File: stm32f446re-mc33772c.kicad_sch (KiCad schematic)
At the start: 43 parts, among them J1 Conn_01x02, J2 USB_B_Micro, J3 Conn_01x03, J4 Conn_01x03, J6 SM06B-GHS-TB, U1 STM32F446RETx, U3 LD1086D2M33TR, U4 AMS1117-3.3, U6 LMR51450SDRRR, U7 SN65HVD232, Y1 16MHz

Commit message: no error in DRC
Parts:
- J1: footprint Connector_PinHeader_1.00mm:PinHeader_1x02_P1.00mm_Vertical -> Connector_PinHeader_2.54mm:PinHeader_1x02_P2.54mm_Vertical
- J3, J4: footprint Connector_PinHeader_1.00mm:PinHeader_1x03_P1.00mm_Vertical -> Connector_PinHeader_2.54mm:PinHeader_1x03_P2.54mm_Vertical
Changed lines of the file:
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@@
 			)
 		)
-		(property "Footprint" "Connector_PinHeader_1.00mm:PinHeader_1x03_P1.00mm_Vertical"
+		(property "Footprint" "Connector_PinHeader_2.54mm:PinHeader_1x03_P2.54mm_Vertical"
 			(at 148.59 176.53 0)
 			(hide yes)
@@
 			)
 		)
-		(property "Footprint" "Connector_PinHeader_1.00mm:PinHeader_1x02_P1.00mm_Vertical"
+		(property "Footprint" "Connector_PinHeader_2.54mm:PinHeader_1x02_P2.54mm_Vertical"
 			(at 41.91 97.79 0)
 			(hide yes)
@@
 			)
 		)
-		(property "Footprint" "Connector_PinHeader_1.00mm:PinHeader_1x03_P1.00mm_Vertical"
+		(property "Footprint" "Connector_PinHeader_2.54mm:PinHeader_1x03_P2.54mm_Vertical"
 			(at 127 27.94 0)
 			(hide yes)

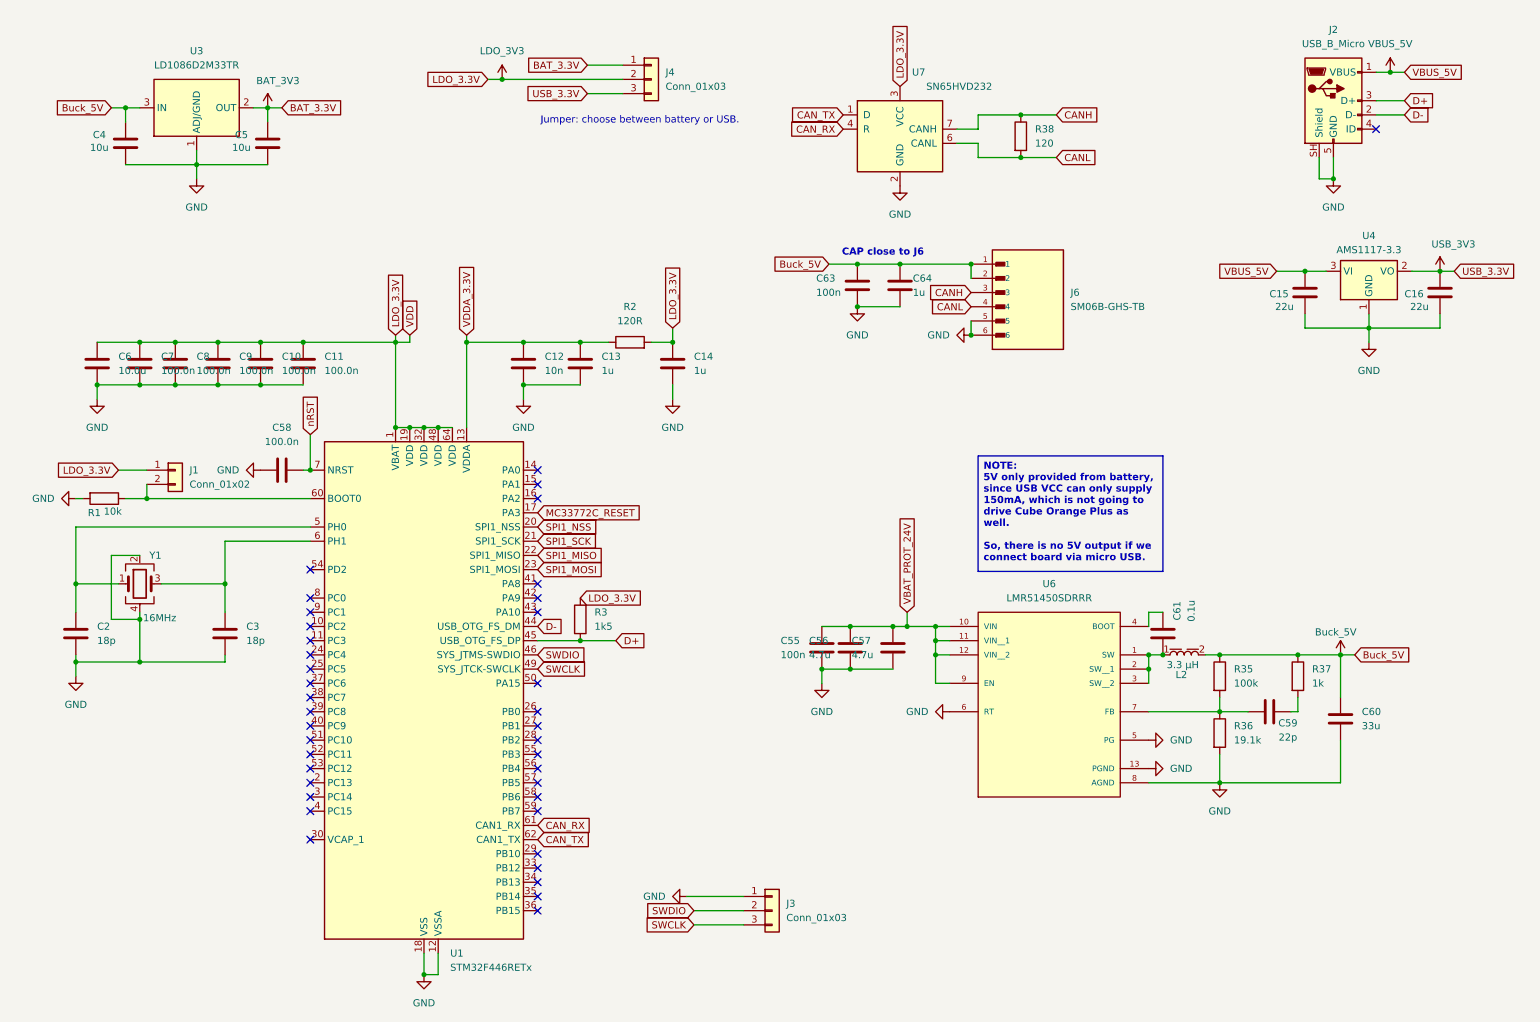
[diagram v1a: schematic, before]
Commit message: add LCPC Part #
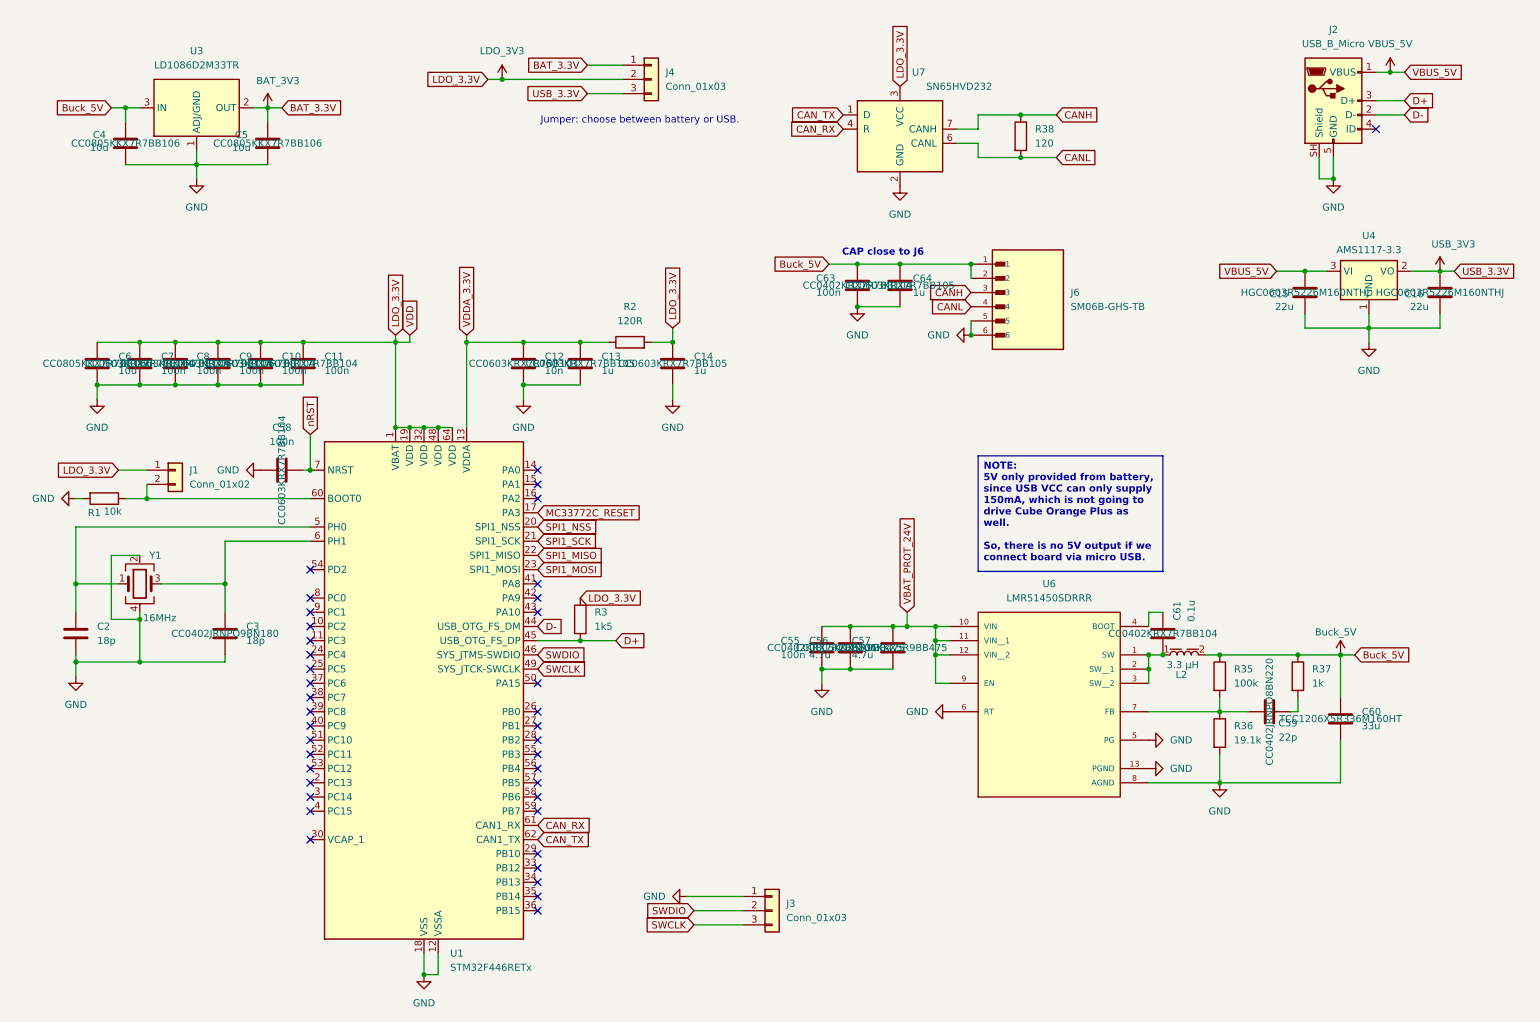
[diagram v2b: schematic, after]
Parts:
- C10, C11, C58, C7, C8, C9: value 100.0n -> 100n; LCSC Part # (none) -> CC0603KRX7R7BB104
- C12: LCSC Part # (none) -> CC0603KRX7R7BB103
- C13, C14, C64: LCSC Part # (none) -> CC0603KRX7R7BB105
- C15, C16: footprint Capacitor_SMD:C_0402_1005Metric -> Capacitor_SMD:C_0603_1608Metric; LCSC Part # (none) -> HGC0603R5226M160NTHJ
- C2, C3: LCSC Part # (none) -> CC0402JRNPO9BN180
- C4, C5: LCSC Part # (none) -> CC0805KKX7R7BB106
- C55, C61, C63: LCSC Part # (none) -> CC0402KRX7R7BB104
- C56, C57: LCSC Part # (none) -> CC0805KKX5R9BB475
- C59: LCSC Part # (none) -> CC0402JRNPO8BN220
- C6: value 10.0u -> 10u; LCSC Part # (none) -> CC0805KKX7R7BB106
- C60: LCSC Part # (none) -> TCC1206X5R336M160HT

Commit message: update for JLCPCB with LCSC part #
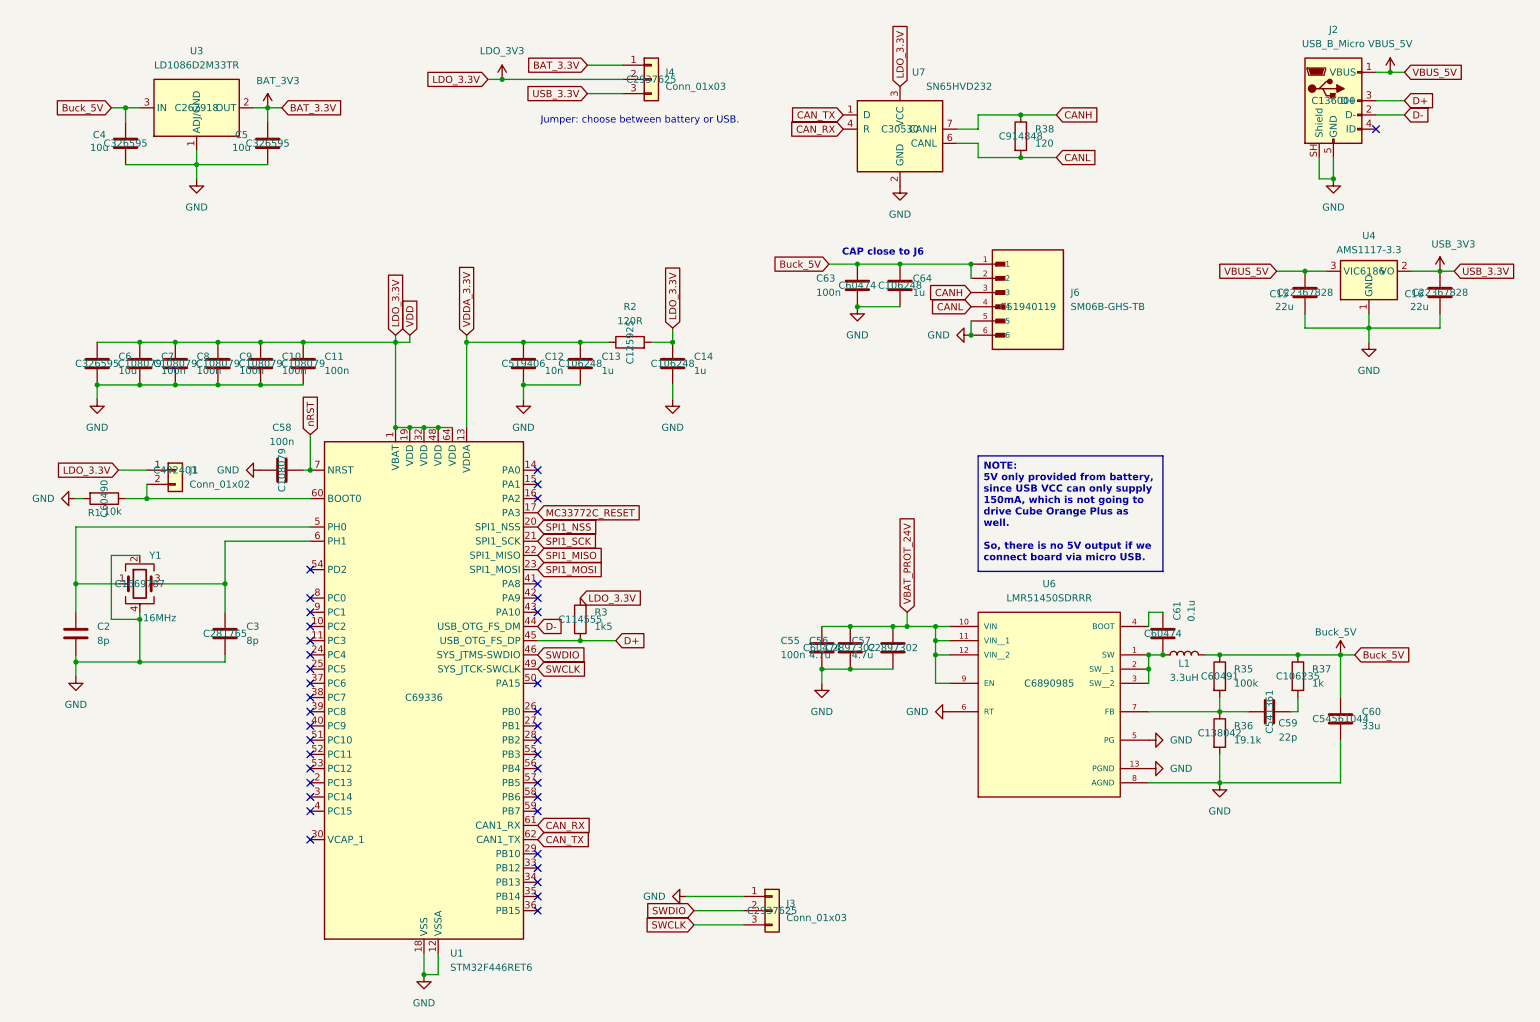
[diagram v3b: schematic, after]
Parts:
- removed L2: 1040_74437368033, MyFootLib:L_Wurth_WE-LHMI-1040, symbol MyySym:1040_74437368033
- added L1: 3.3uH, MyFootLib:PSPMAA0605H-3R3M-ANP, symbol Device:L
- C10, C11, C58, C7, C8, C9: LCSC Part # CC0603KRX7R7BB104 -> C108079
- C12: LCSC Part # CC0603KRX7R7BB103 -> C519406
- C13, C14, C64: LCSC Part # CC0603KRX7R7BB105 -> C106248
- C15, C16: LCSC Part # HGC0603R5226M160NTHJ -> C22367828
- C2, C3: value 18p -> 8p; LCSC Part # CC0402JRNPO9BN180 -> C281765
- C4, C5, C6: LCSC Part # CC0805KKX7R7BB106 -> C326595
- C55, C61, C63: LCSC Part # CC0402KRX7R7BB104 -> C60474
- C56, C57: LCSC Part # CC0805KKX5R9BB475 -> C2897302
- C59: LCSC Part # CC0402JRNPO8BN220 -> C541361
- C60: LCSC Part # TCC1206X5R336M160HT -> C54561044
- J1: LCSC Part # (none) -> C492401
- J2: LCSC Part # (none) -> C136000
- J3, J4: LCSC Part # (none) -> C2937625
- J6: LCSC Part # (none) -> C51940119
- R1: LCSC Part # (none) -> C60490
- R2: LCSC Part # (none) -> C125925
- R3: LCSC Part # (none) -> C114555
- R35: LCSC Part # (none) -> C60491
- R36: LCSC Part # (none) -> C138042
- R37: LCSC Part # (none) -> C106235
- R38: LCSC Part # (none) -> C914848
- U1: value STM32F446RETx -> STM32F446RET6; LCSC Part # (none) -> C69336
- U3: LCSC Part # (none) -> C262918
- U4: LCSC Part # (none) -> C6186
- U6: LCSC Part # (none) -> C6890985
- U7: LCSC Part # (none) -> C30530
- Y1: LCSC Part # (none) -> C1669787
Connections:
- net Buck_5V: now also L1.2
- net at C61.2, U6.1 (SW), U6.2 (SW__1)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: now also L1.1

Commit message: export to JLCPCB
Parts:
- C61: value 0.1u -> 100n
- J1, J3, J4: FT Rotation Offset (none) -> 90
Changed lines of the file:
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@@
 			)
 		)
-		(property "Value" "0.1u"
+		(property "Value" "100n"
 			(at 223.52 122.936 90)
 			(show_name no)
@@
 			)
 		)
+		(property "FT Rotation Offset" "90"
+			(at 148.59 176.53 0)
+			(hide yes)
+			(show_name no)
+			(do_not_autoplace no)
+			(effects
+				(font
+					(size 1.27 1.27)
+				)
+			)
+		)
 		(pin "1"
 		)
@@
 			)
 		)
+		(property "FT Rotation Offset" "90"
+			(at 41.91 97.79 0)
+			(hide yes)
+			(show_name no)
+			(do_not_autoplace no)
+			(effects
+				(font
+					(size 1.27 1.27)
+				)
+			)
+		)
 		(pin "1"
 		)
@@
 			(show_name no)
 			(do_not_autoplace no)
+			(effects
+				(font
+					(size 1.27 1.27)
+				)
+			)
+		)
+		(property "FT Rotation Offset" "90"
+			(at 127 27.94 0)
+			(hide yes)
+			(show_name no)
+			(do_not_autoplace no)

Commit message: for PCBWay
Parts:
- C10, C11, C58, C7, C8, C9: MPN (none) -> CC0603KRX7R7BB104
- C12: MPN (none) -> CC0603KRX7R7BB103
- C13, C14, C64: MPN (none) -> CC0603KRX7R7BB105
- C15, C16: MPN (none) -> HGC0603R5226M160NTHJ
- C2, C3: MPN (none) -> CC0402BRNPO9BN8R0
- C4, C5, C6: MPN (none) -> CC0805KKX7R7BB106
- C55, C61, C63: MPN (none) -> CC0402KRX7R7BB104
- C56, C57: MPN (none) -> CC0805KKX5R9BB475
- C59: MPN (none) -> CC0402JRNPO8BN220
- C60: MPN (none) -> TCC1206X5R336M160HT
- J1: MPN (none) -> PZ254V-11-02P
- J2: MPN (none) -> 1050170001
- J3, J4: MPN (none) -> PZ254V-11-03P
- J6: MPN (none) -> XY-SM06B-GHS-TB
- L1: MPN (none) -> PSPMAA0605H-3R3M-ANP
- R1: MPN (none) -> RC0402FR-0710KL
- R2: MPN (none) -> AC0603FR-07120RL
- R3: MPN (none) -> RC0805FR-071K5L
- R35: MPN (none) -> RC0402FR-07100KL
- R36: MPN (none) -> RC0402FR-0719K1L
- R37: MPN (none) -> RC0402FR-071KL
- R38: MPN (none) -> RC1206FR-7W120RL
- U1: MPN (none) -> STM32F446RET6
- U3: MPN (none) -> LD1086D2M33TR
- U4: MPN (none) -> AMS1117-3.3
- U6: MPN (none) -> LMR51450SDRRR
- U7: MPN (none) -> SN65HVD232DR
- Y1: MPN (none) -> ABM8AIG-16.000MHZ-82Z-T

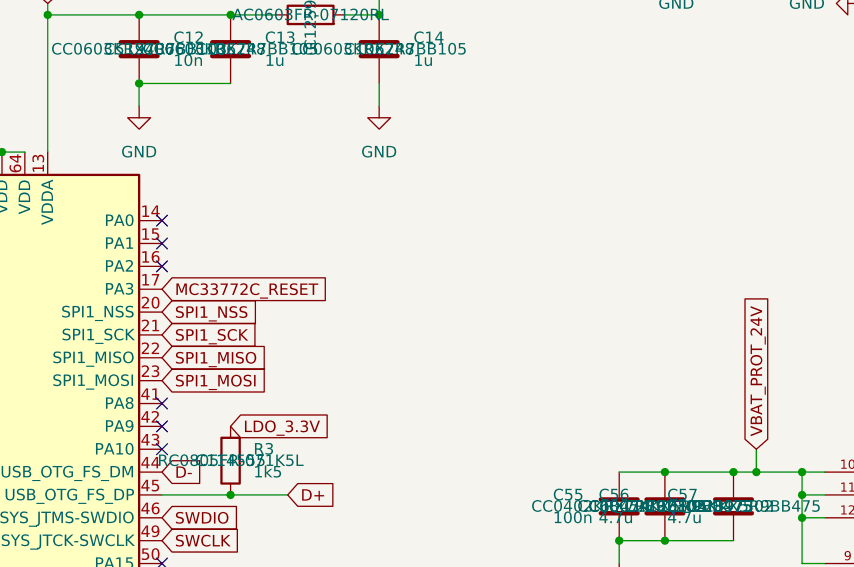
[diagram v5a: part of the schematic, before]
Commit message: add testpoint
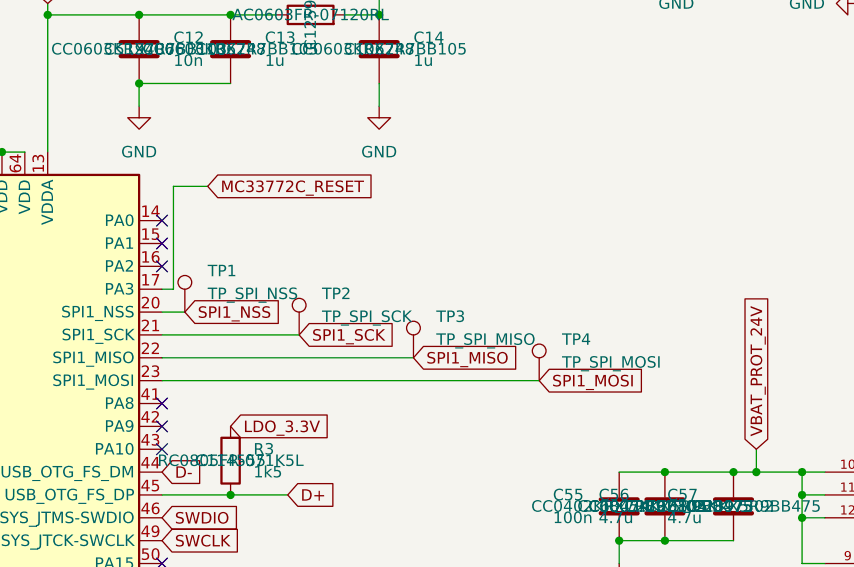
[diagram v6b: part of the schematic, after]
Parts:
- added TP1: TP_SPI_NSS, TestPoint:TestPoint_Pad_D1.0mm, symbol Connector:TestPoint
- added TP2: TP_SPI_SCK, TestPoint:TestPoint_Pad_D1.0mm, symbol Connector:TestPoint
- added TP3: TP_SPI_MISO, TestPoint:TestPoint_Pad_D1.0mm, symbol Connector:TestPoint
- added TP4: TP_SPI_MOSI, TestPoint:TestPoint_Pad_D1.0mm, symbol Connector:TestPoint
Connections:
- net SPI1_MISO: now also TP3.1
- net SPI1_MOSI: now also TP4.1
- net SPI1_NSS: now also TP1.1
- net SPI1_SCK: now also TP2.1
